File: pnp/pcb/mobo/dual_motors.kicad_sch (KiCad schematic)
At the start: 9 parts, among them M5 MOTOR1, M6 MOTOR2

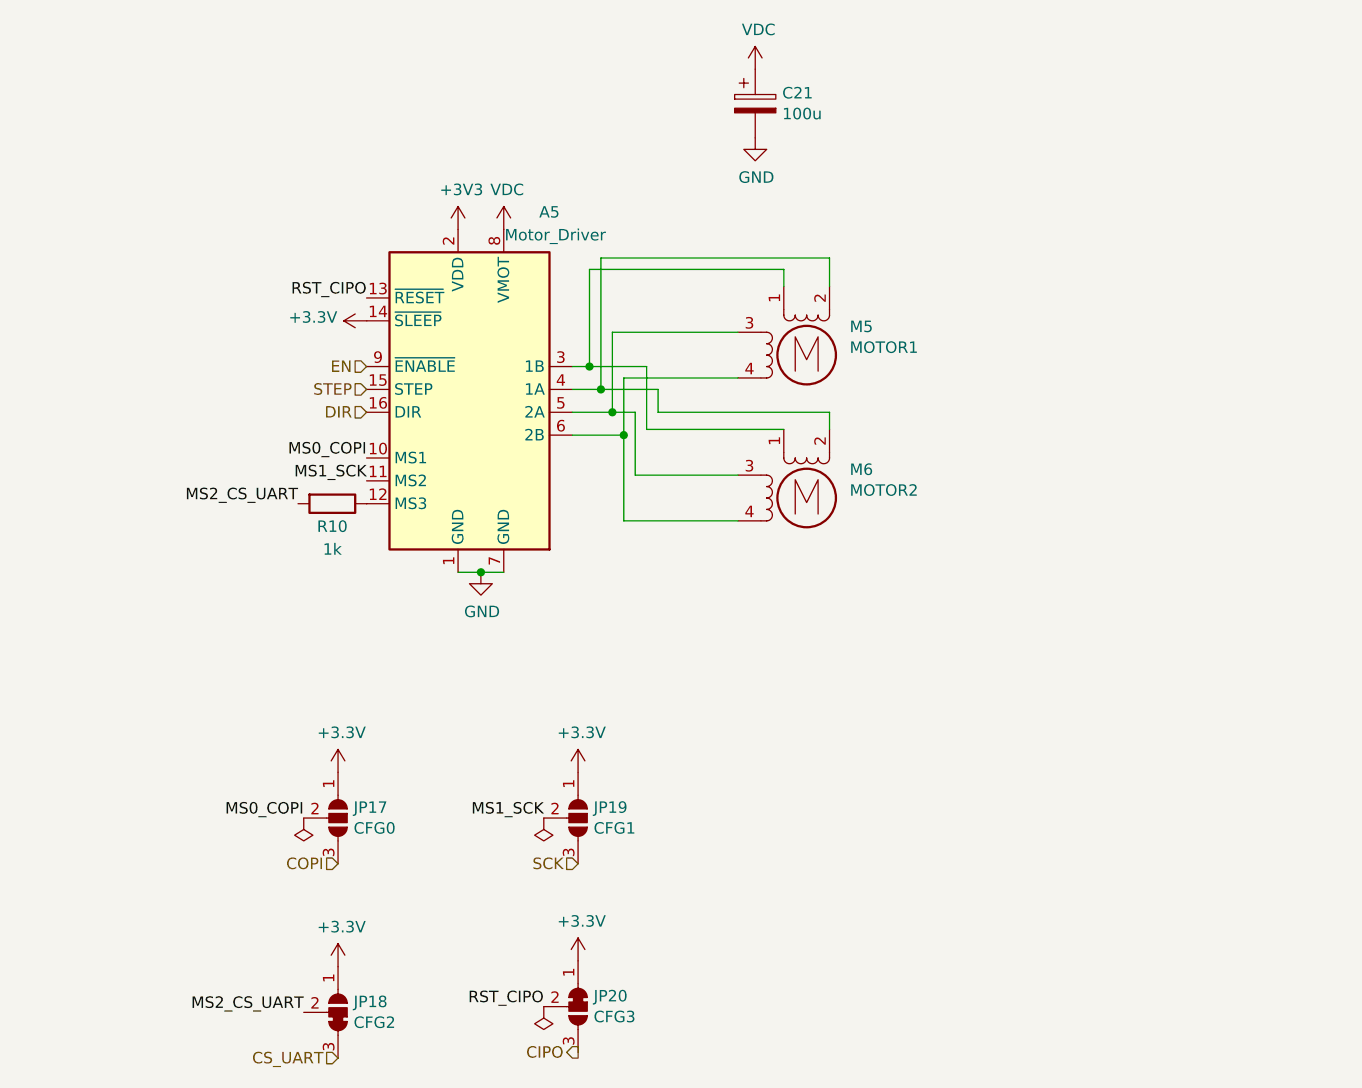
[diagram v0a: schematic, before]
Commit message: Clean the ERC
- Changed some broken symbol links
- Changed all _Limit netlabels to _LIMIT

ERC list is now empty.
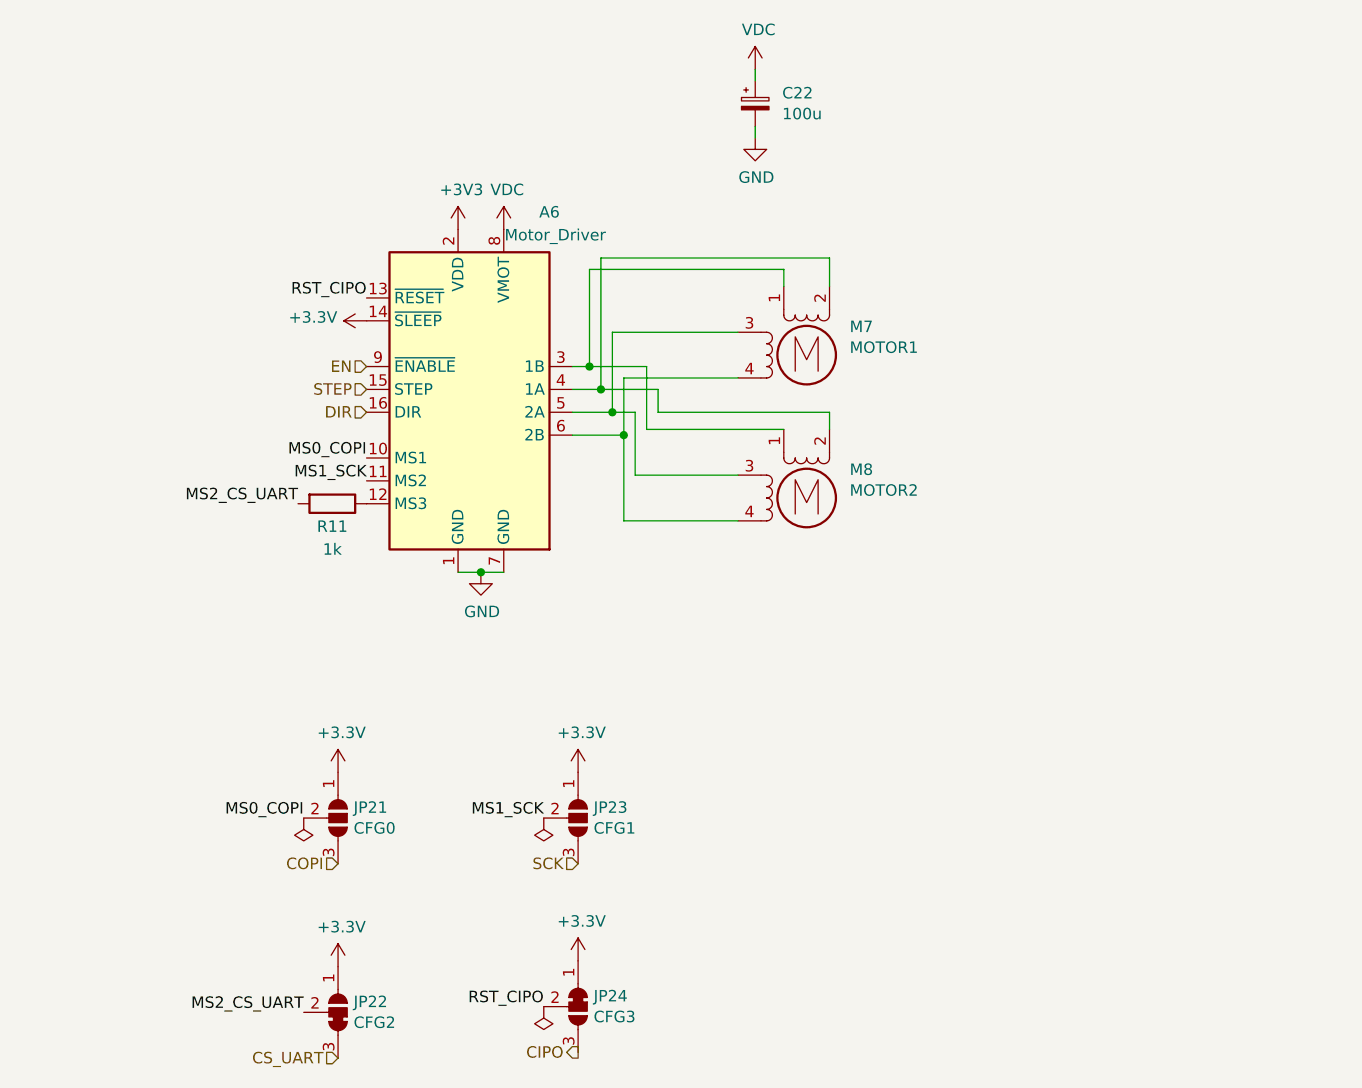
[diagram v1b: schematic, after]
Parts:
- C22: renamed from C21; symbol Device:CP -> Device:C_Polarized_Small
- renumbered A5 to A6, JP17 to JP21, JP18 to JP22, JP19 to JP23, JP20 to JP24, M5 to M7, M6 to M8, R10 to R11
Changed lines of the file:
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@@
+    (stroke (width 0) (type default) (color 0 0 0 0))
+  )
+  (wire (pts (xy 165.735 44.45) (xy 165.735 45.72))
     (stroke (width 0) (type default) (color 0 0 0 0))
   )
@@
   )
   (wire (pts (xy 173.99 82.55) (xy 154.94 82.55))
+    (stroke (width 0) (type default) (color 0 0 0 0))
+  )
+  (wire (pts (xy 165.735 50.8) (xy 165.735 52.07))
     (stroke (width 0) (type default) (color 0 0 0 0))
   )
@@
   (symbol (lib_id "Motor:Stepper_Motor_bipolar") (at 171.45 92.075 0)
     (in_bom yes) (on_board yes)
-    (property "Reference" "M6" (id 0) (at 176.2252 88.9254 0)
+    (property "Reference" "M8" (id 0) (at 176.2252 88.9254 0)
       (effects (font (size 1.27 1.27)) (justify left))
     )
@@
   (symbol (lib_id "Motor:Stepper_Motor_bipolar") (at 171.45 76.2 0)
     (in_bom yes) (on_board yes)
-    (property "Reference" "M5" (id 0) (at 176.2252 73.0504 0)
+    (property "Reference" "M7" (id 0) (at 176.2252 73.0504 0)
       (effects (font (size 1.27 1.27)) (justify left))
     )
@@
   (symbol (lib_id "Driver_Motor:Pololu_Breakout_A4988") (at 132.715 80.01 0)
     (in_bom yes) (on_board yes)
-    (property "Reference" "A5" (id 0) (at 142.875 60.325 0))
+    (property "Reference" "A6" (id 0) (at 142.875 60.325 0))
     (property "Value" "Motor_Driver" (id 1) (at 143.51 62.865 0))
     (property "Footprint" "Module:Pololu_Breakout-16_15.2x20.3mm" (id 2) (at 139.7 99.06 0)
@@
     (pin "1")
   )
-  (symbol (lib_id "Device:CP") (at 165.735 48.26 0)
-    (in_bom yes) (on_board yes)
-    (property "Reference" "C21" (id 0) (at 168.7322 47.0916 0)
+  (symbol (lib_id "Device:C_Polarized_Small") (at 165.735 48.26 0)
+    (in_bom yes) (on_board yes)
+    (property "Reference" "C22" (id 0) (at 168.7322 47.0916 0)
       (effects (font (size 1.27 1.27)) (justify left))
     )
@@
   (symbol (lib_id "Jumper:SolderJumper_3_Open") (at 119.38 127.635 270)
     (in_bom yes) (on_board yes)
-    (property "Reference" "JP17" (id 0) (at 121.1072 126.4666 90)
+    (property "Reference" "JP21" (id 0) (at 121.1072 126.4666 90)
       (effects (font (size 1.27 1.27)) (justify left))
     )
@@
   (symbol (lib_id "Jumper:SolderJumper_3_Bridged12") (at 146.05 148.59 270)
     (in_bom yes) (on_board yes)
-    (property "Reference" "JP20" (id 0) (at 147.7772 147.4216 90)
+    (property "Reference" "JP24" (id 0) (at 147.7772 147.4216 90)
       (effects (font (size 1.27 1.27)) (justify left))
     )
@@
   (symbol (lib_id "Jumper:SolderJumper_3_Open") (at 146.05 127.635 270)
     (in_bom yes) (on_board yes)
-    (property "Reference" "JP19" (id 0) (at 147.7772 126.4666 90)
+    (property "Reference" "JP23" (id 0) (at 147.7772 126.4666 90)
       (effects (font (size 1.27 1.27)) (justify left))
     )
@@
   (symbol (lib_id "Device:R") (at 118.745 92.71 270)
     (in_bom yes) (on_board yes)
-    (property "Reference" "R10" (id 0) (at 118.745 95.25 90))
+    (property "Reference" "R11" (id 0) (at 118.745 95.25 90))
     (property "Value" "1k" (id 1) (at 118.745 97.79 90))
     (property "Footprint" "Resistor_SMD:R_0805_2012Metric" (id 2) (at 118.745 90.932 90)
@@
   (symbol (lib_id "index:SolderJumper_3_Bridged23") (at 119.38 149.225 270) (mirror x)
     (in_bom yes) (on_board yes)
-    (property "Reference" "JP18" (id 0) (at 121.1072 148.0566 90)
-      (effects (font (size 1.27 1.27)) (justify left))
-    )
+    (property "Reference" "JP22" (id 0) (at 121.1072 148.0566 90)
+      (effects (font (size 1.27 1.27)) (justify left))
+    )

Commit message: Create a hierarchical structure
Put all circuits in to a single-function sheet
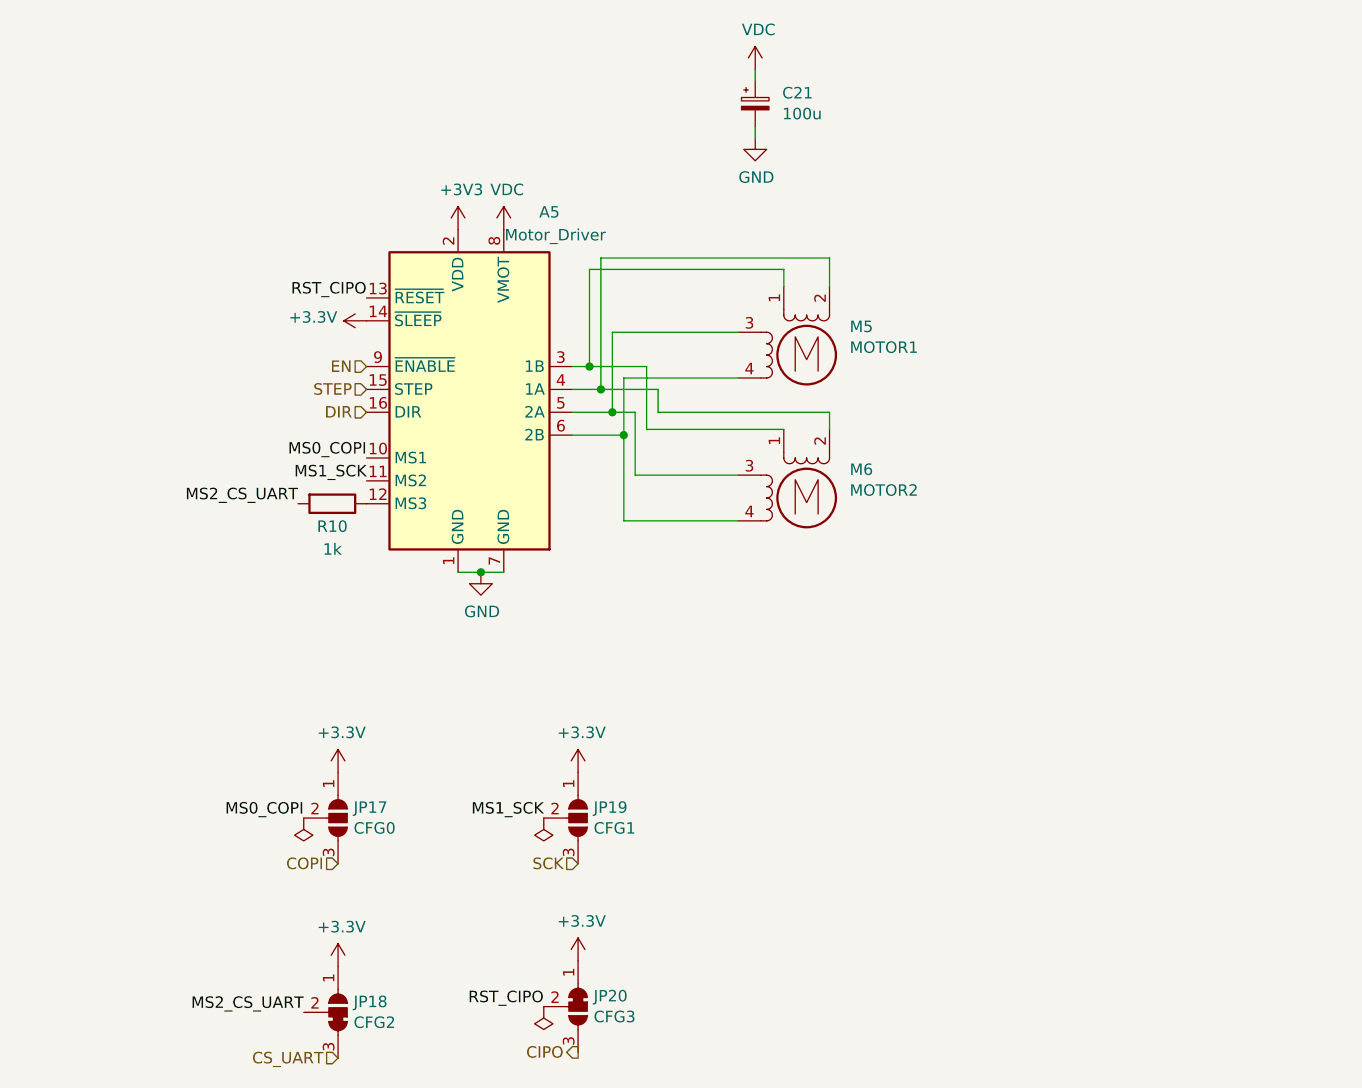
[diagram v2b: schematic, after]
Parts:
- renumbered A6 to A5, C22 to C21, JP21 to JP17, JP22 to JP18, JP23 to JP19, JP24 to JP20, M7 to M5, M8 to M6, R11 to R10
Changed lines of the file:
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@@
   (symbol (lib_id "Motor:Stepper_Motor_bipolar") (at 171.45 92.075 0)
     (in_bom yes) (on_board yes)
-    (property "Reference" "M8" (id 0) (at 176.2252 88.9254 0)
+    (property "Reference" "M6" (id 0) (at 176.2252 88.9254 0)
       (effects (font (size 1.27 1.27)) (justify left))
     )
@@
   (symbol (lib_id "Motor:Stepper_Motor_bipolar") (at 171.45 76.2 0)
     (in_bom yes) (on_board yes)
-    (property "Reference" "M7" (id 0) (at 176.2252 73.0504 0)
+    (property "Reference" "M5" (id 0) (at 176.2252 73.0504 0)
       (effects (font (size 1.27 1.27)) (justify left))
     )
@@
   (symbol (lib_id "Driver_Motor:Pololu_Breakout_A4988") (at 132.715 80.01 0)
     (in_bom yes) (on_board yes)
-    (property "Reference" "A6" (id 0) (at 142.875 60.325 0))
+    (property "Reference" "A5" (id 0) (at 142.875 60.325 0))
     (property "Value" "Motor_Driver" (id 1) (at 143.51 62.865 0))
     (property "Footprint" "Module:Pololu_Breakout-16_15.2x20.3mm" (id 2) (at 139.7 99.06 0)
@@
   (symbol (lib_id "Device:C_Polarized_Small") (at 165.735 48.26 0)
     (in_bom yes) (on_board yes)
-    (property "Reference" "C22" (id 0) (at 168.7322 47.0916 0)
+    (property "Reference" "C21" (id 0) (at 168.7322 47.0916 0)
       (effects (font (size 1.27 1.27)) (justify left))
     )
@@
   (symbol (lib_id "Jumper:SolderJumper_3_Open") (at 119.38 127.635 270)
     (in_bom yes) (on_board yes)
-    (property "Reference" "JP21" (id 0) (at 121.1072 126.4666 90)
+    (property "Reference" "JP17" (id 0) (at 121.1072 126.4666 90)
       (effects (font (size 1.27 1.27)) (justify left))
     )
@@
   (symbol (lib_id "Jumper:SolderJumper_3_Bridged12") (at 146.05 148.59 270)
     (in_bom yes) (on_board yes)
-    (property "Reference" "JP24" (id 0) (at 147.7772 147.4216 90)
+    (property "Reference" "JP20" (id 0) (at 147.7772 147.4216 90)
       (effects (font (size 1.27 1.27)) (justify left))
     )
@@
   (symbol (lib_id "Jumper:SolderJumper_3_Open") (at 146.05 127.635 270)
     (in_bom yes) (on_board yes)
-    (property "Reference" "JP23" (id 0) (at 147.7772 126.4666 90)
+    (property "Reference" "JP19" (id 0) (at 147.7772 126.4666 90)
       (effects (font (size 1.27 1.27)) (justify left))
     )
@@
   (symbol (lib_id "Device:R") (at 118.745 92.71 270)
     (in_bom yes) (on_board yes)
-    (property "Reference" "R11" (id 0) (at 118.745 95.25 90))
+    (property "Reference" "R10" (id 0) (at 118.745 95.25 90))
     (property "Value" "1k" (id 1) (at 118.745 97.79 90))
     (property "Footprint" "Resistor_SMD:R_0805_2012Metric" (id 2) (at 118.745 90.932 90)
@@
   (symbol (lib_id "index:SolderJumper_3_Bridged23") (at 119.38 149.225 270) (mirror x)
     (in_bom yes) (on_board yes)
-    (property "Reference" "JP22" (id 0) (at 121.1072 148.0566 90)
-      (effects (font (size 1.27 1.27)) (justify left))
-    )
+    (property "Reference" "JP18" (id 0) (at 121.1072 148.0566 90)
+      (effects (font (size 1.27 1.27)) (justify left))
+    )

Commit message: All sheets cleaned up
All symbols and their fields are now neatly organized.

All hierarchical pins are already imported,
except for the microcontroller sheet.
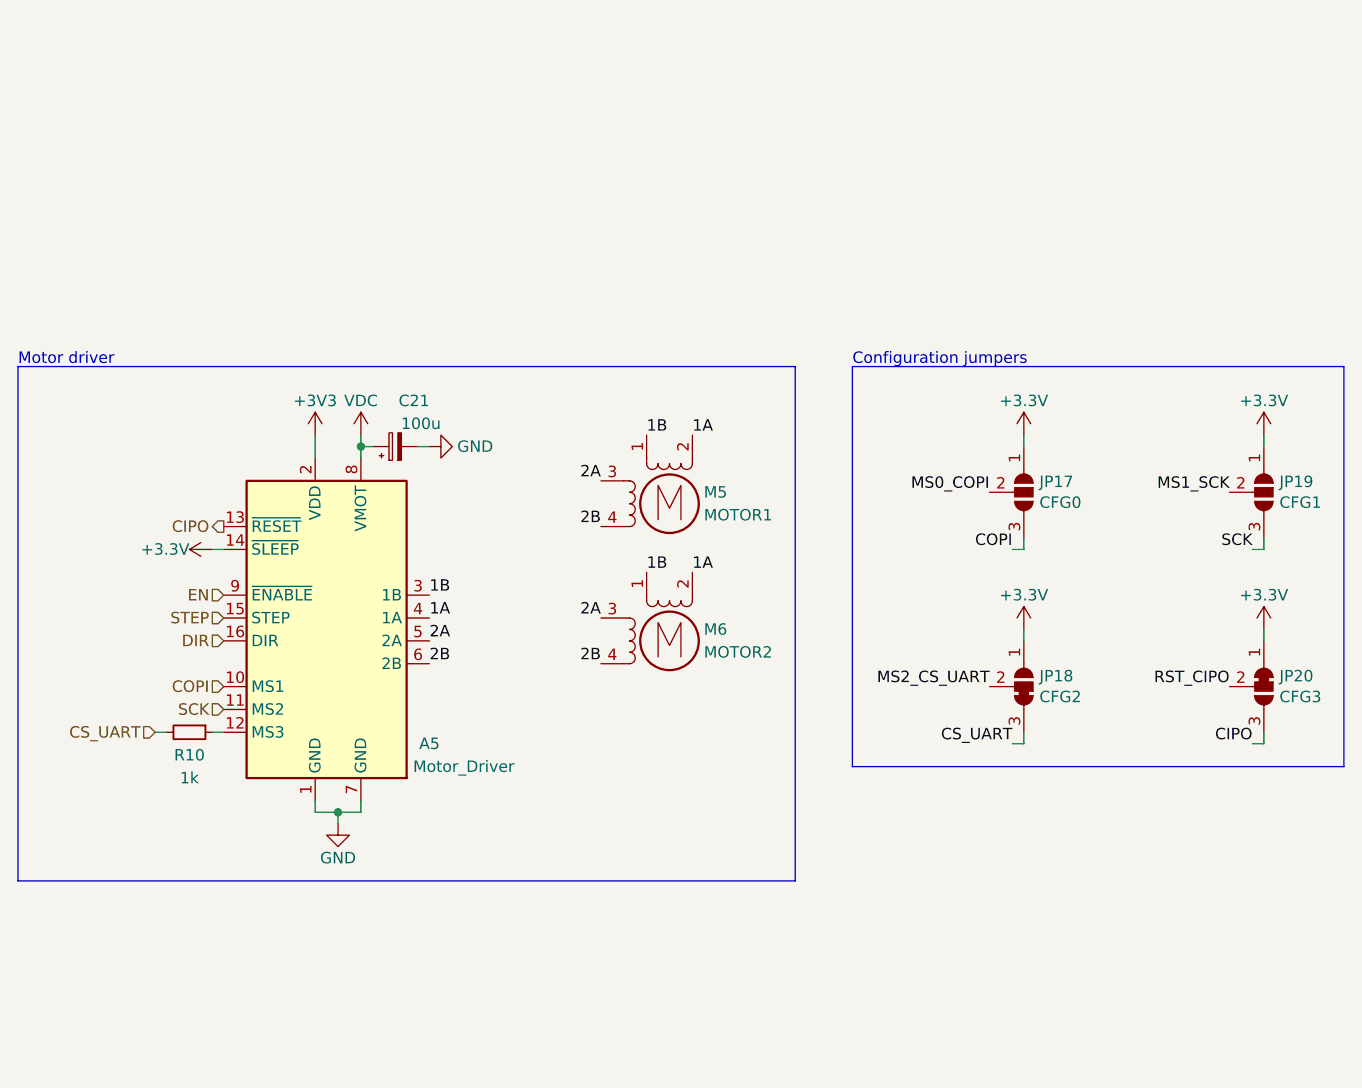
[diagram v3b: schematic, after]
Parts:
- R10: symbol Device:R -> Device:R_Small
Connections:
- net CIPO: now also A5.13 (~{RESET})
- net COPI: now also A5.10 (MS1)
- net CS_UART: now also R10.2
- net MS0_COPI: no longer A5.10 (MS1)
- net MS1_SCK: no longer A5.11 (MS2)
- net MS2_CS_UART: no longer R10.2
- net RST_CIPO: no longer A5.13 (~{RESET})
- net SCK: now also A5.11 (MS2)
- net 1B: now reaches A5.3 (1B), M5.1, M6.1
- net 1A: now reaches A5.4 (1A), M5.2 (-), M6.2 (-)
- net 2A: now reaches A5.5 (2A), M5.3, M6.3
- net 2B: now reaches A5.6 (2B), M5.4, M6.4
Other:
- note added: "Configuration jumpers"
- note added: "Motor driver"
- moved on the sheet: A5, C21, JP17, JP18, JP19, JP20, M5, M6, R10
